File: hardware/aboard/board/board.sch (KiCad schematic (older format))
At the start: 8 parts, among them P1 Power, P2 Analog, P3 Digital, P4 Digital, P5 CONN_01X01, P6 CONN_01X01, P7 CONN_01X01, P8 CONN_01X01

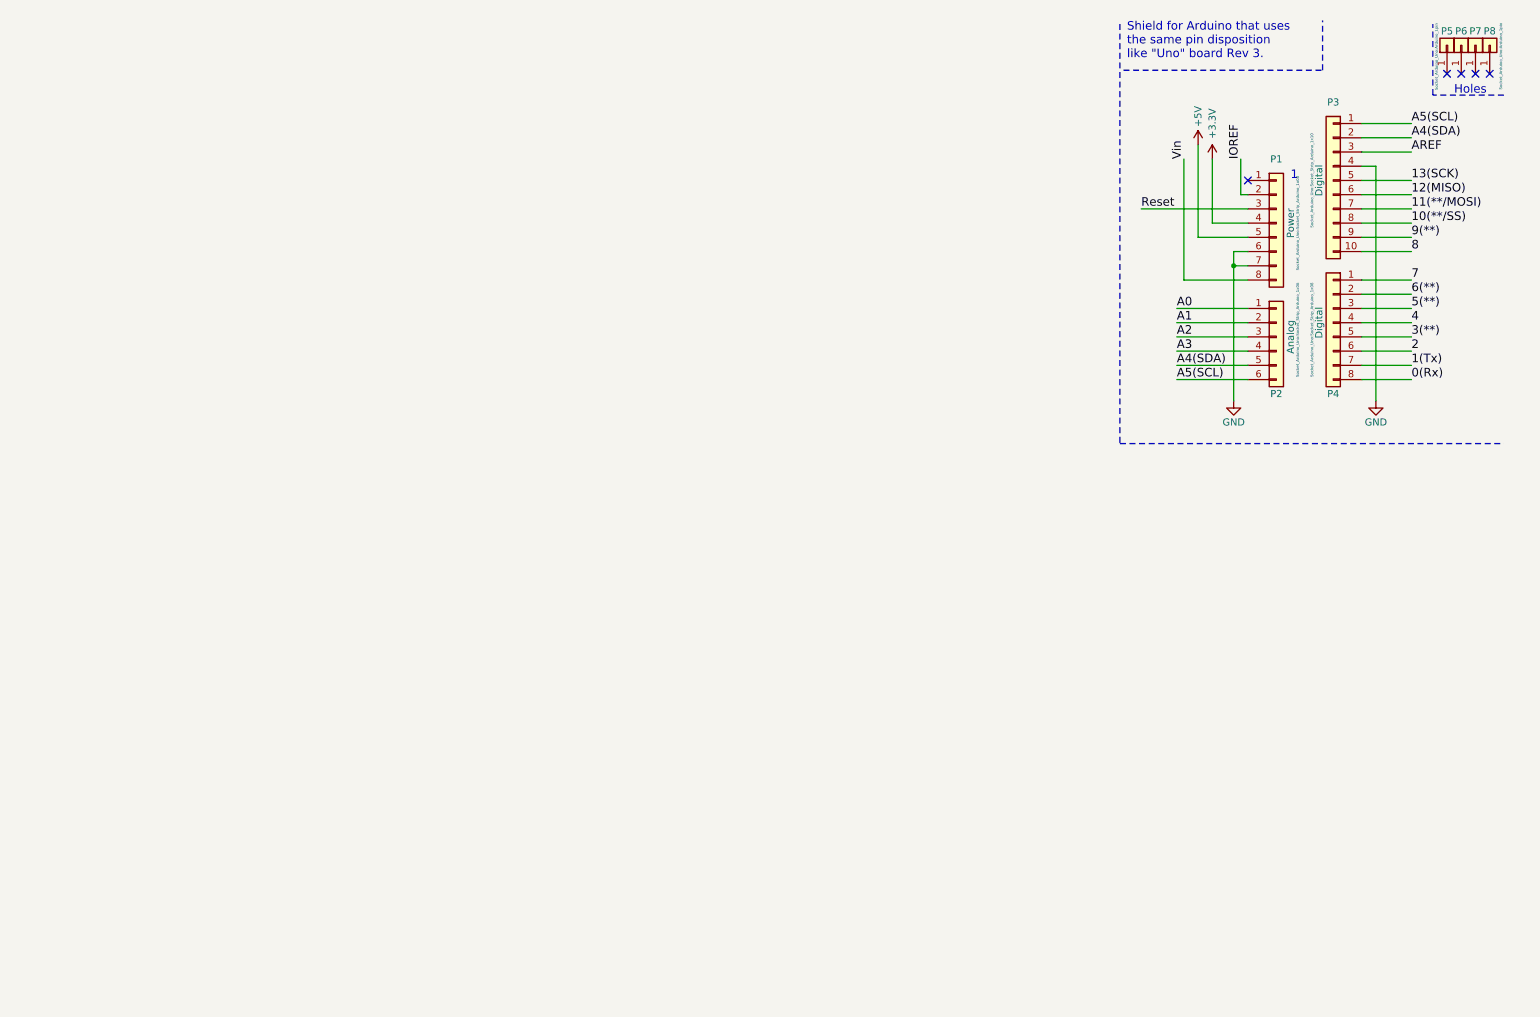
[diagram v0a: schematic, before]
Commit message: board for OM13088UL started-2
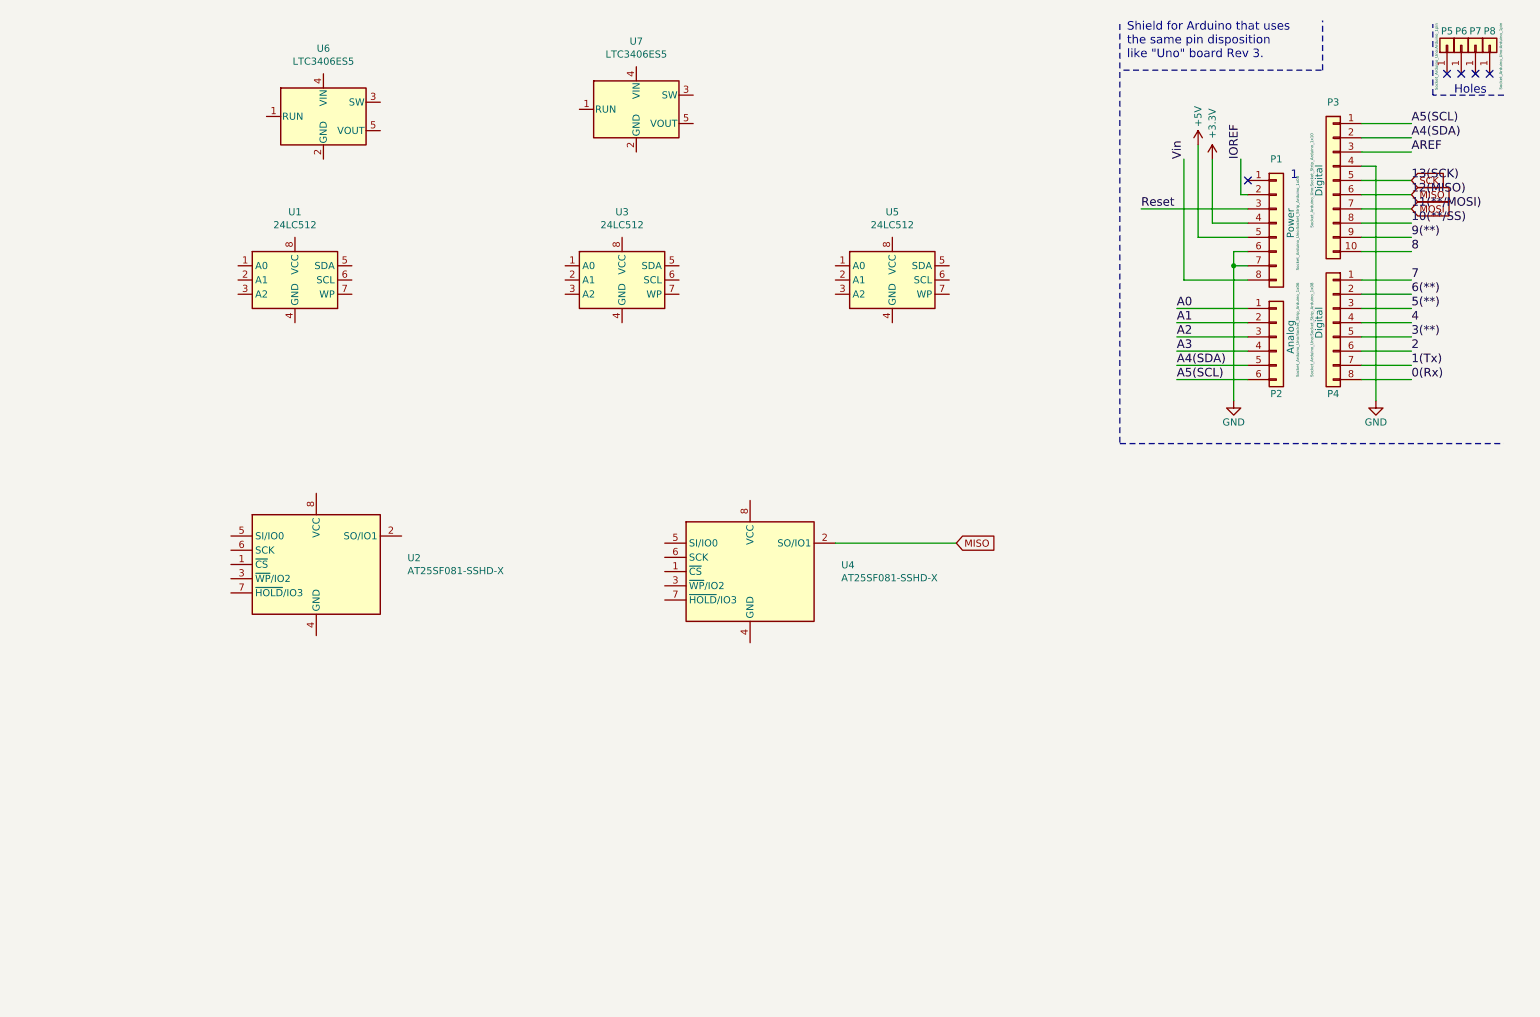
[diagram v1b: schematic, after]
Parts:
- added U1, U3, U5: 24LC512, symbol Memory_EEPROM:24LC512
- added U2, U4: AT25SF081-SSHD-X, Package_SO:SOIC-8_3.9x4.9mm_P1.27mm, symbol Memory_Flash:AT25SF081-SSHD-X
- added U6, U7: LTC3406ES5, Package_TO_SOT_SMD:TSOT-23-5, symbol Regulator_Switching:LTC3406ES5
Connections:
- net 11(**/MOSI) renamed MOSI
- net 12(MISO) renamed MISO
- net MISO: now also U4.2 (SO/IO1)
- net 13(SCK) renamed SCK
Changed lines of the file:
@@
 EESchema Schematic File Version 4
-LIBS:Arduino_As_Uno-cache
+LIBS:board-cache
 EELAYER 26 0
 EELAYER END
@@
 Wire Notes Line
 	10700 1000 10700 500
+$Comp
+L Memory_EEPROM:24LC512 U3
+U 1 1 5D38B189
+P 5000 2300
+F 0 "U3" H 5000 2778 50  0000 C CNN
+F 1 "24LC512" H 5000 2687 50  0000 C CNN
+F 2 "" H 5000 2300 50  0001 C CNN
+F 3 "http://ww1.microchip.com/downloads/en/DeviceDoc/21754M.pdf" H 5000 2300 50  0001 C CNN
+	1    5000 2300
+	1    0    0    -1
+$EndComp
+$Comp
+L Memory_EEPROM:24LC512 U1
+U 1 1 5D38B245
+P 2700 2300
+F 0 "U1" H 2700 2778 50  0000 C CNN
+F 1 "24LC512" H 2700 2687 50  0000 C CNN
+F 2 "" H 2700 2300 50  0001 C CNN
+F 3 "http://ww1.microchip.com/downloads/en/DeviceDoc/21754M.pdf" H 2700 2300 50  0001 C CNN
+	1    2700 2300
+	1    0    0    -1
+$EndComp
+$Comp
+L Memory_EEPROM:24LC512 U5
+U 1 1 5D38B2D7
+P 6900 2300
+F 0 "U5" H 6900 2778 50  0000 C CNN
+F 1 "24LC512" H 6900 2687 50  0000 C CNN
+F 2 "" H 6900 2300 50  0001 C CNN
+F 3 "http://ww1.microchip.com/downloads/en/DeviceDoc/21754M.pdf" H 6900 2300 50  0001 C CNN
+	1    6900 2300
+	1    0    0    -1
+$EndComp
+$Comp
+L Memory_Flash:AT25SF081-SSHD-X U2
+U 1 1 5D38CE55
+P 2850 4300
+F 0 "U2" H 3491 4346 50  0000 L CNN
+F 1 "AT25SF081-SSHD-X" H 3491 4255 50  0000 L CNN
+F 2 "Package_SO:SOIC-8_3.9x4.9mm_P1.27mm" H 2850 3700 50  0001 C CNN
+F 3 "https://www.adestotech.com/wp-content/uploads/DS-AT25SF081_045.pdf" H 2850 4300 50  0001 C CNN
+	1    2850 4300
+	1    0    0    -1
+$EndComp
+$Comp
+L Memory_Flash:AT25SF081-SSHD-X U4
+U 1 1 5D38CF09
+P 5900 4350
+F 0 "U4" H 6541 4396 50  0000 L CNN
+F 1 "AT25SF081-SSHD-X" H 6541 4305 50  0000 L CNN
+F 2 "Package_SO:SOIC-8_3.9x4.9mm_P1.27mm" H 5900 3750 50  0001 C CNN
+F 3 "https://www.adestotech.com/wp-content/uploads/DS-AT25SF081_045.pdf" H 5900 4350 50  0001 C CNN
+	1    5900 4350
+	1    0    0    -1
+$EndComp
+Wire Wire Line
+	6500 4150 7350 4150
+Text GLabel 7350 4150 2    50   Input ~ 0
+MISO
+Text GLabel 10550 1700 2    50   Input ~ 0
+MISO
+Text GLabel 10550 1800 2    50   Input ~ 0
+MOSI
+Text GLabel 10550 1600 2    50   Input ~ 0
+SCK
+$Comp
+L Regulator_Switching:LTC3406ES5 U6
+U 1 1 5D38F742
+P 2900 1150
+F 0 "U6" H 2900 1628 50  0000 C CNN
+F 1 "LTC3406ES5" H 2900 1537 50  0000 C CNN
+F 2 "Package_TO_SOT_SMD:TSOT-23-5" H 3600 900 50  0001 C CNN
+F 3 "http://cds.linear.com/docs/en/datasheet/3406b12fs.pdf" H 2900 1100 50  0001 C CNN
+	1    2900 1150
+	1    0    0    -1
+$EndComp
+$Comp
+L Regulator_Switching:LTC3406ES5 U7
+U 1 1 5D38F7E0
+P 5100 1100
+F 0 "U7" H 5100 1578 50  0000 C CNN
+F 1 "LTC3406ES5" H 5100 1487 50  0000 C CNN
+F 2 "Package_TO_SOT_SMD:TSOT-23-5" H 5800 850 50  0001 C CNN
+F 3 "http://cds.linear.com/docs/en/datasheet/3406b12fs.pdf" H 5100 1050 50  0001 C CNN
+	1    5100 1100
+	1    0    0    -1
+$EndComp
 $EndSCHEMATC

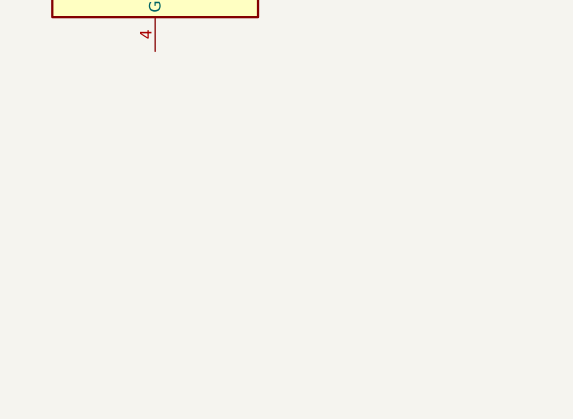
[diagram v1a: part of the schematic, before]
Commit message: board for OM13088UL started library
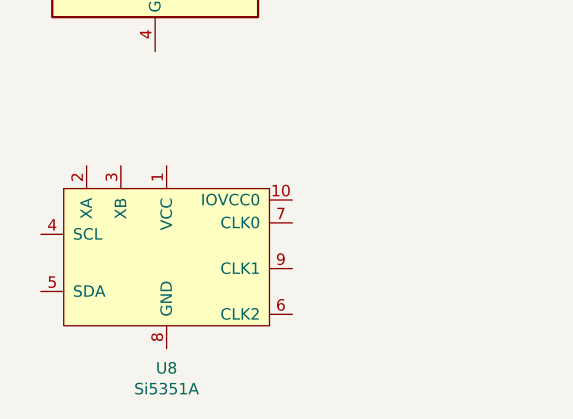
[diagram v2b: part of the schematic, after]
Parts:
- added U8: Si5351A, symbol kilib:Si5351A
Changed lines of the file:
@@
+	1    0    0    -1
+$EndComp
+$Comp
+L kilib:Si5351A U8
+U 1 1 5D392F3E
+P 2900 5550
+F 0 "U8" H 2900 4914 50  0000 C CNN
+F 1 "Si5351A" H 2900 4823 50  0000 C CNN
+F 2 "" H 2900 5550 50  0001 C CNN
+F 3 "" H 2900 5550 50  0001 C CNN
+	1    2900 5550
 	1    0    0    -1
 $EndComp

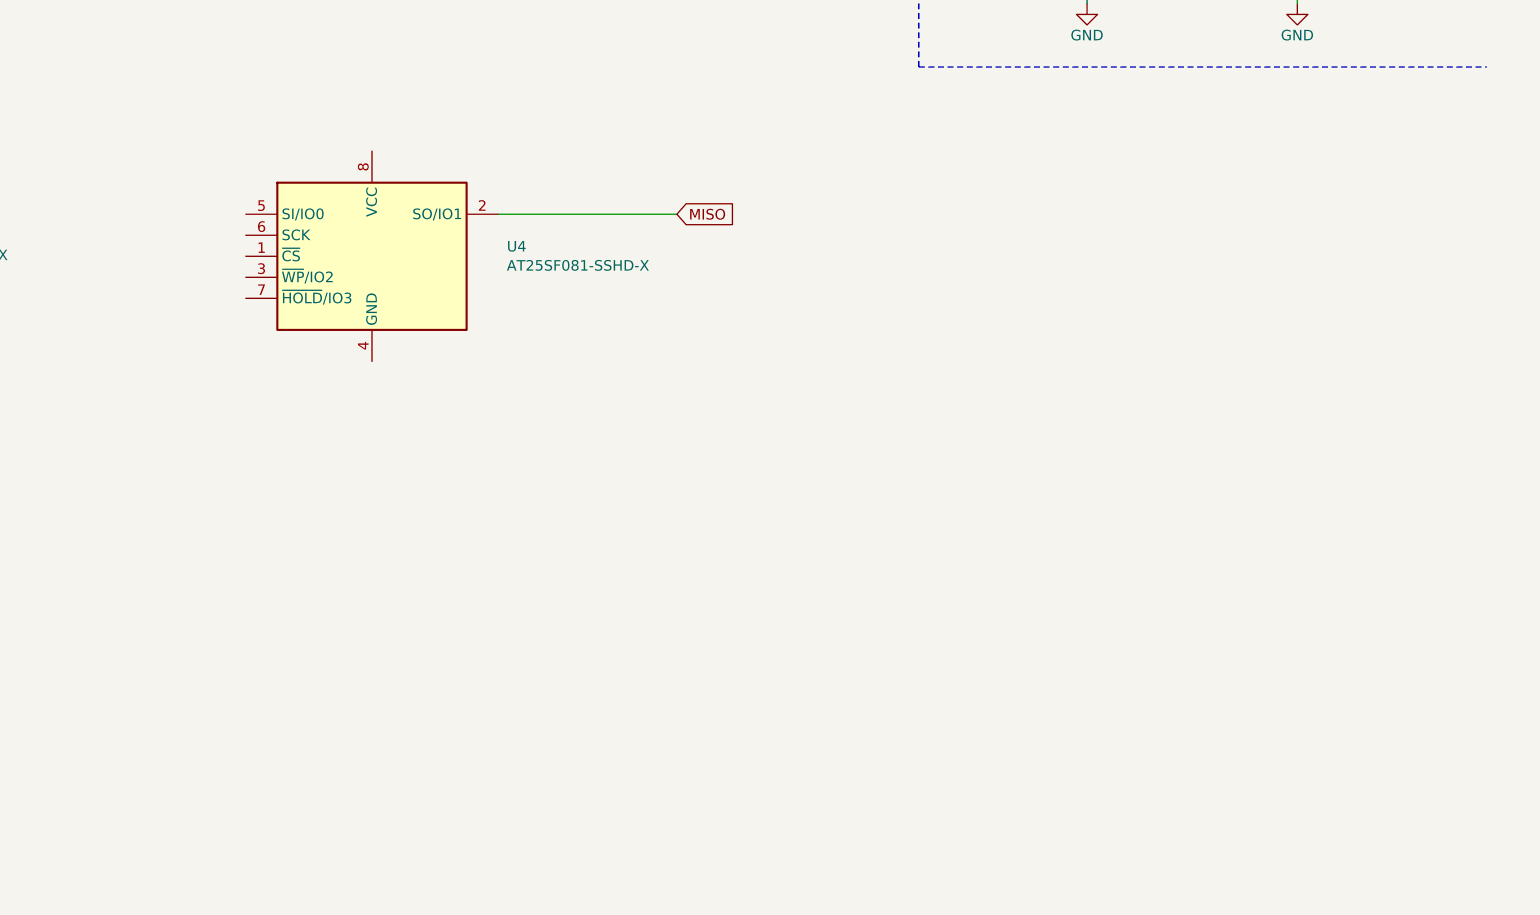
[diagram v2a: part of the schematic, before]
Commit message: board for OM13088UL: ST25DV04K symbol
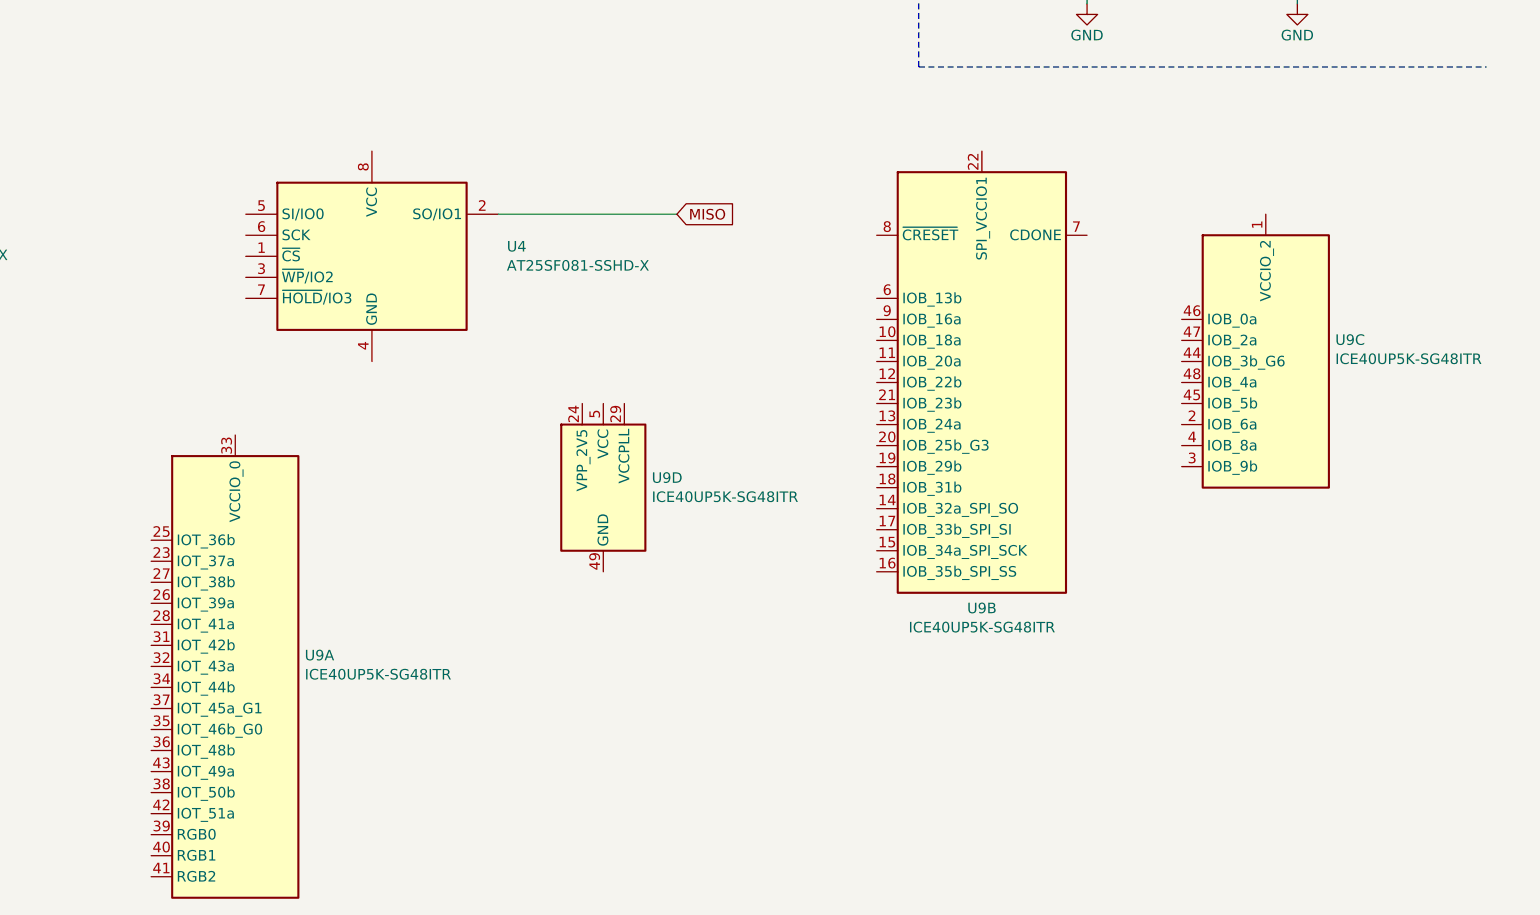
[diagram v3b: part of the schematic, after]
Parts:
- added U9: ICE40UP5K-SG48ITR, Package_DFN_QFN:QFN-48-1EP_7x7mm_P0.5mm_EP5.6x5.6mm, symbol FPGA_Lattice:ICE40UP5K-SG48ITR
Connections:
- new net: U9.30 (VCC), U9.5 (VCC)
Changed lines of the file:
@@
+	1    0    0    -1
+$EndComp
+$Comp
+L FPGA_Lattice:ICE40UP5K-SG48ITR U9
+U 1 1 5D3948B4
+P 5250 6300
+F 0 "U9" H 5580 6352 50  0000 L CNN
+F 1 "ICE40UP5K-SG48ITR" H 5580 6261 50  0000 L CNN
+F 2 "Package_DFN_QFN:QFN-48-1EP_7x7mm_P0.5mm_EP5.6x5.6mm" H 5250 4950 50  0001 C CNN
+F 3 "http://www.latticesemi.com/Products/FPGAandCPLD/iCE40Ultra" H 4850 7300 50  0001 C CNN
+	1    5250 6300
+	1    0    0    -1
+$EndComp
+$Comp
+L FPGA_Lattice:ICE40UP5K-SG48ITR U9
+U 2 1 5D394DFC
+P 8800 4950
+F 0 "U9" H 8800 3876 50  0000 C CNN
+F 1 "ICE40UP5K-SG48ITR" H 8800 3785 50  0000 C CNN
+F 2 "Package_DFN_QFN:QFN-48-1EP_7x7mm_P0.5mm_EP5.6x5.6mm" H 8800 3600 50  0001 C CNN
+F 3 "http://www.latticesemi.com/Products/FPGAandCPLD/iCE40Ultra" H 8400 5950 50  0001 C CNN
+	2    8800 4950
+	1    0    0    -1
+$EndComp
+$Comp
+L FPGA_Lattice:ICE40UP5K-SG48ITR U9
+U 3 1 5D394EF5
+P 10150 4850
+F 0 "U9" H 10480 4952 50  0000 L CNN
+F 1 "ICE40UP5K-SG48ITR" H 10480 4861 50  0000 L CNN
+F 2 "Package_DFN_QFN:QFN-48-1EP_7x7mm_P0.5mm_EP5.6x5.6mm" H 10150 3500 50  0001 C CNN
+F 3 "http://www.latticesemi.com/Products/FPGAandCPLD/iCE40Ultra" H 9750 5850 50  0001 C CNN
+	3    10150 4850
+	1    0    0    -1
+$EndComp
+$Comp
+L FPGA_Lattice:ICE40UP5K-SG48ITR U9
+U 4 1 5D394F99
+P 7000 5450
+F 0 "U9" H 7230 5496 50  0000 L CNN
+F 1 "ICE40UP5K-SG48ITR" H 7230 5405 50  0000 L CNN
+F 2 "Package_DFN_QFN:QFN-48-1EP_7x7mm_P0.5mm_EP5.6x5.6mm" H 7000 4100 50  0001 C CNN
+F 3 "http://www.latticesemi.com/Products/FPGAandCPLD/iCE40Ultra" H 6600 6450 50  0001 C CNN
+	4    7000 5450
 	1    0    0    -1
 $EndComp

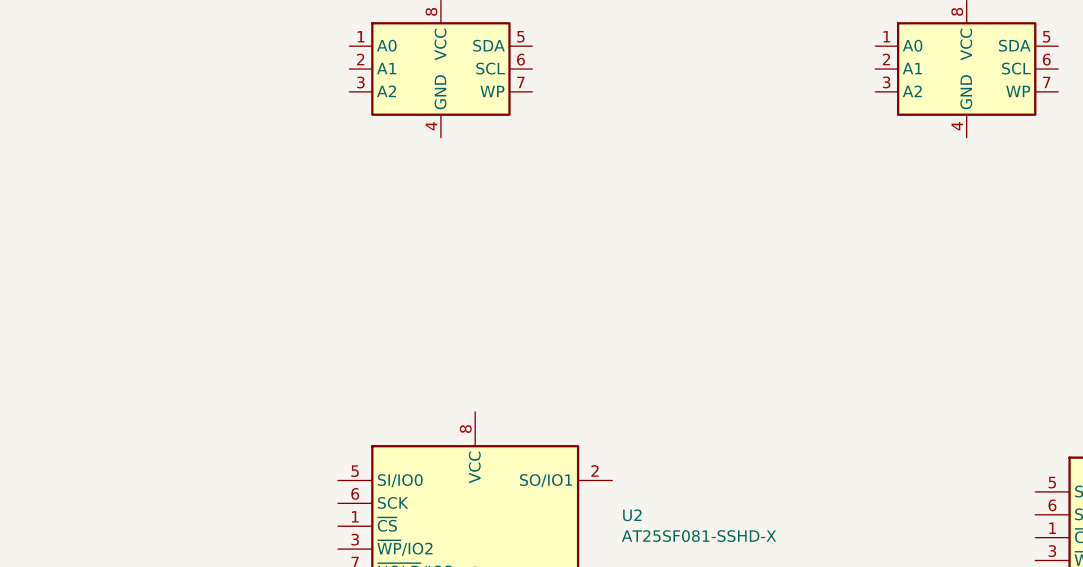
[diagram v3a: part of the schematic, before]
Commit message: board for OM13088UL: ST25DV04K symbol
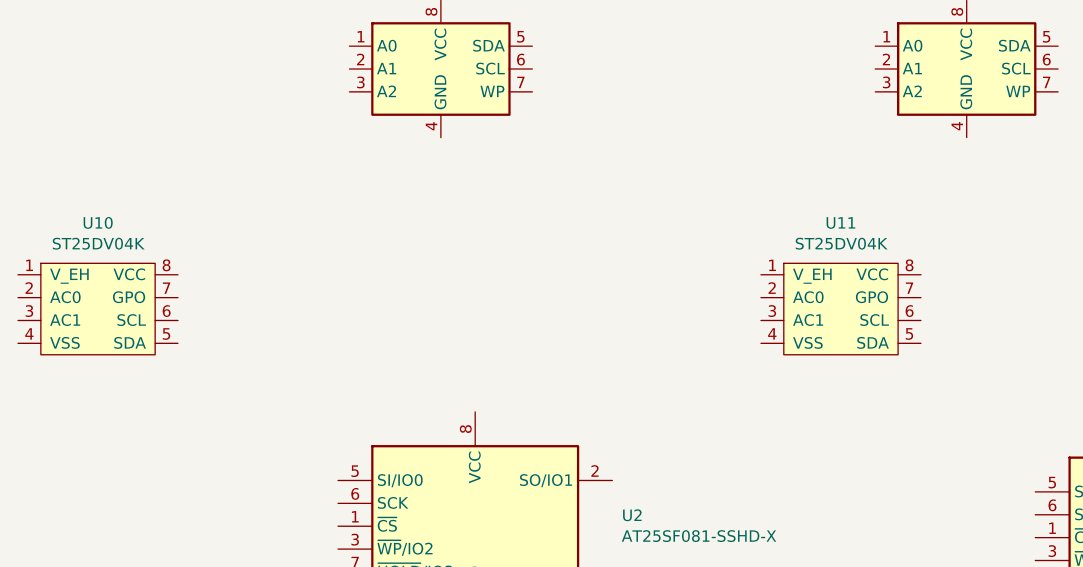
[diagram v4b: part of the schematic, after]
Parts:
- added U10, U11: ST25DV04K, symbol kilib:ST25DV04K
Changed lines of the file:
@@
+	1    0    0    -1
+$EndComp
+$Comp
+L kilib:ST25DV04K U10
+U 1 1 5D394CBB
+P 1200 3350
+F 0 "U10" H 1200 3725 50  0000 C CNN
+F 1 "ST25DV04K" H 1200 3634 50  0000 C CNN
+F 2 "" H 1200 3350 50  0001 C CNN
+F 3 "" H 1200 3350 50  0001 C CNN
+	1    1200 3350
+	1    0    0    -1
+$EndComp
+$Comp
+L kilib:ST25DV04K U11
+U 1 1 5D394D62
+P 4450 3350
+F 0 "U11" H 4450 3725 50  0000 C CNN
+F 1 "ST25DV04K" H 4450 3634 50  0000 C CNN
+F 2 "" H 4450 3350 50  0001 C CNN
+F 3 "" H 4450 3350 50  0001 C CNN
+	1    4450 3350
 	1    0    0    -1
 $EndComp
